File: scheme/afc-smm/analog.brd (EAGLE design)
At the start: 80 x 80 mm, 89 parts, among them IC1 OP1177R, IC10 LM2931-5.0, IC11 OP184, IC12 DAC8551, IC13 REF3033, IC14 317EMP, IC15 317EMP, IC2 TL082D, IC3 AD8515RJ, IC4 AD8615RJ, IC5 AD8221R, IC6 AD7476, IC7 REF3033, IC8 LM337LM, IC9 317EMP, J1 22-27-2031-03, J2 22-27-2021-02, Q1 IRLML2803, X1 BNC-206, X2 BNC-206

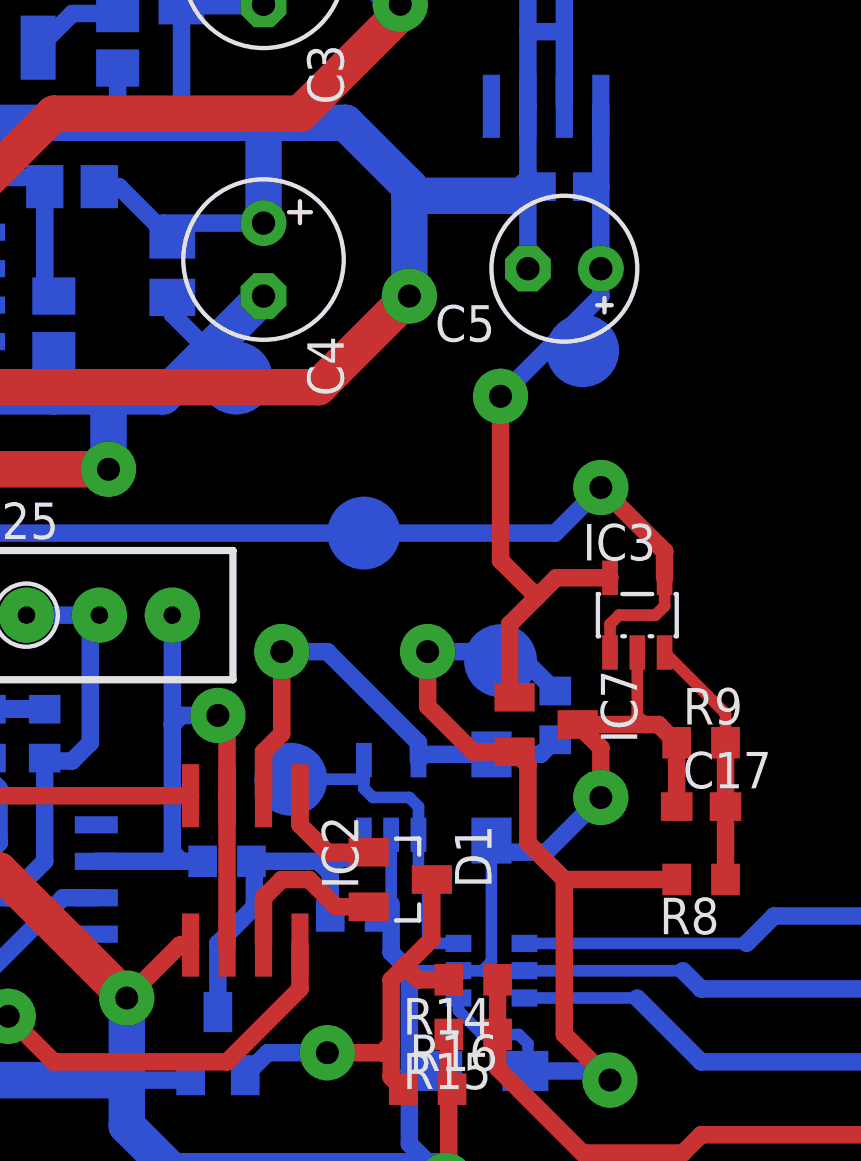
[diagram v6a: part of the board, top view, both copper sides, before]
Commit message: some bugfix after assembly, not all bugfix yet (capacitor for example and ground in dac)
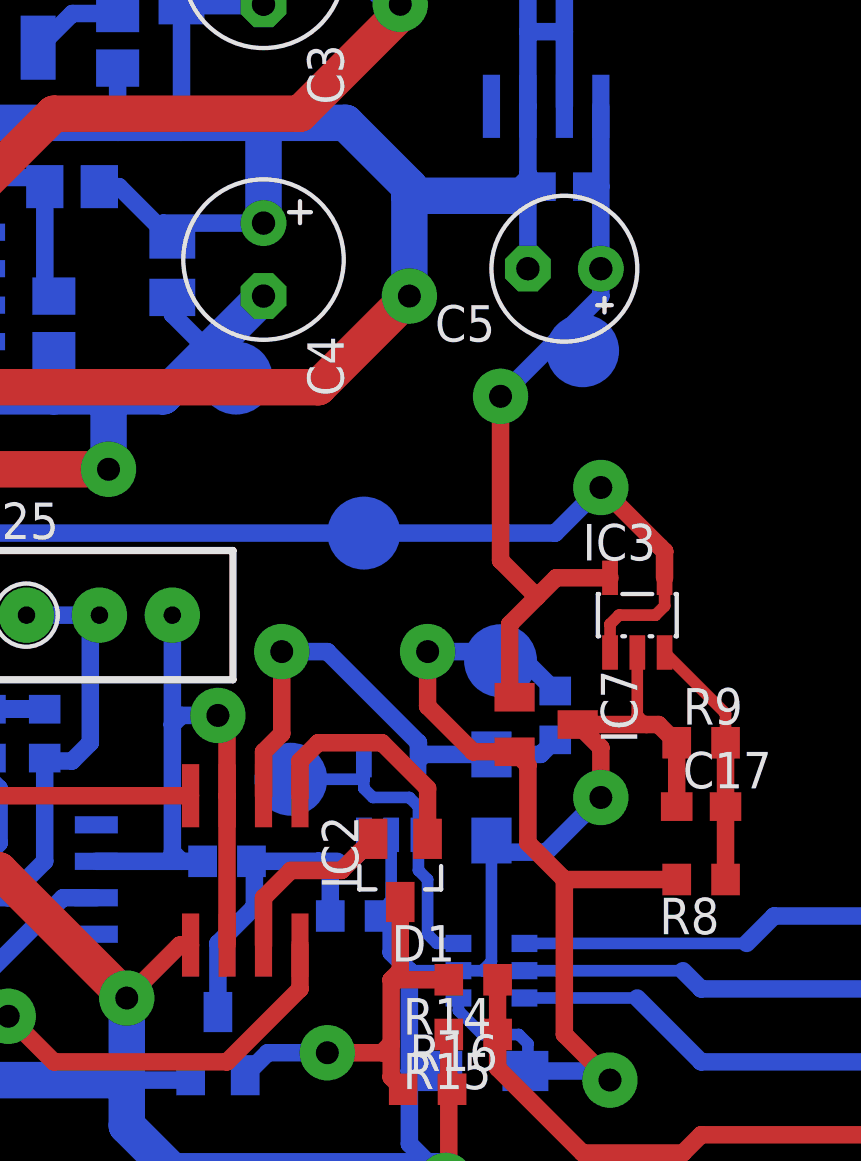
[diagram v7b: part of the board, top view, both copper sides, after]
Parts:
- moved D1 0.32 mm to (52.4, 42.5), turned to 180 degrees
- turned C8 to 0 degrees
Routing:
- net N$4: track 3.80 -> 8.33 mm
- net N$5: track 15.3 -> 14.4 mm
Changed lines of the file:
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@@
 <element name="IC1" library="linear" package="SOIC8" value="OP1177R" x="39.0525" y="42.2275" rot="MR90"/>
 <element name="IC2" library="linear" package="SO08" value="TL082D" x="46.99" y="42.545" rot="R180"/>
-<element name="D1" library="diode" package="SOT23" value="BAT54C" x="52.3875" y="42.2275" rot="R270"/>
+<element name="D1" library="diode" package="SOT23" value="BAT54C" x="52.3875" y="42.545" rot="R180"/>
 <element name="IC3" library="afc-smm" package="SOT23-5" value="AD8515RJ" x="60.6425" y="51.435">
 <attribute name="OC_NEWARK" value="88H0268" x="80.9625" y="-3.175" size="1.778" layer="27" display="off"/>
@@
 <element name="Q1" library="afc-smm" package="SOT23" value="IRLML2803" x="46.0375" y="36.5125" rot="MR0"/>
 <element name="C16" library="rcl" package="C0603" value="0.1" x="31.115" y="46.0375" rot="MR180"/>
-<element name="C8" library="rcl" package="C0603" value="0.1" x="58.1025" y="66.3575" rot="MR180"/>
+<element name="C8" library="rcl" package="C0603" value="0.1" x="58.1025" y="66.3575" rot="MR0"/>
 <element name="C12" library="rcl" package="C0603" value="0.1" x="62.5475" y="4.445" rot="MR270"/>
 <element name="C17" library="rcl" package="C0603" value="0.1" x="62.865" y="44.7675"/>
@@
 <wire x1="73.025" y1="63.3857" x2="72.6694" y2="63.7413" width="0.6096" layer="1"/>
 <contactref element="C8" pad="2"/>
-<wire x1="56.88375" y1="66.72625" x2="58.9525" y2="66.3575" width="0" layer="19" extent="16-16"/>
+<wire x1="57.2525" y1="66.3575" x2="56.8325" y2="66.3575" width="0.4064" layer="16"/>
 </signal>
 <signal name="N$1">
@@
 <contactref element="D1" pad="3"/>
 <contactref element="R14" pad="2"/>
-<wire x1="53.4875" y1="42.2275" x2="53.4875" y2="40.1525" width="0.6096" layer="1"/>
-<wire x1="53.4875" y1="40.1525" x2="52.54625" y2="39.21125" width="0.6096" layer="1"/>
-<wire x1="52.54625" y1="39.21125" x2="52.07" y2="38.735" width="0.6096" layer="1"/>
 <via x="49.8475" y="36.195" extent="1-16" drill="0.8" diameter="1.9304"/>
 <wire x1="52.07" y1="38.735" x2="52.07" y2="36.5125" width="0.6096" layer="1"/>
 <wire x1="52.07" y1="36.5125" x2="52.07" y2="35.345" width="0.6096" layer="1"/>
-<wire x1="54.0775" y1="38.735" x2="53.0225" y2="38.735" width="0.6096" layer="1"/>
-<wire x1="53.0225" y1="38.735" x2="52.54625" y2="39.21125" width="0.6096" layer="1"/>
+<wire x1="54.0775" y1="38.735" x2="52.07" y2="38.735" width="0.6096" layer="1"/>
 <wire x1="52.07" y1="35.345" x2="52.49" y2="34.925" width="0.6096" layer="1"/>
 <wire x1="49.8475" y1="36.195" x2="51.7525" y2="36.195" width="0.6096" layer="1"/>
@@
 <wire x1="49.8475" y1="36.195" x2="47.77" y2="36.195" width="0.6096" layer="16"/>
 <wire x1="47.77" y1="36.195" x2="46.9875" y2="35.4125" width="0.6096" layer="16"/>
+<wire x1="52.3875" y1="41.445" x2="52.3875" y2="39.0525" width="0.6096" layer="1"/>
+<wire x1="52.3875" y1="39.0525" x2="52.07" y2="38.735" width="0.6096" layer="1"/>
 </signal>
 <signal name="N$8">
@@
 <contactref element="D1" pad="1"/>
 <contactref element="IC2" pad="1"/>
-<wire x1="51.2875" y1="43.1775" x2="49.85" y2="43.1775" width="0.6096" layer="1"/>
-<wire x1="49.85" y1="43.1775" x2="48.895" y2="44.1325" width="0.6096" layer="1"/>
-<wire x1="48.895" y1="44.1325" x2="48.895" y2="45.145" width="0.6096" layer="1"/>
+<wire x1="48.895" y1="45.145" x2="48.895" y2="46.355" width="0.6096" layer="1"/>
+<wire x1="48.895" y1="46.355" x2="49.53" y2="46.99" width="0.6096" layer="1"/>
+<wire x1="49.53" y1="46.99" x2="51.7525" y2="46.99" width="0.6096" layer="1"/>
+<wire x1="51.7525" y1="46.99" x2="53.34" y2="45.4025" width="0.6096" layer="1"/>
+<wire x1="53.34" y1="45.4025" x2="53.34" y2="43.6475" width="0.6096" layer="1"/>
+<wire x1="53.34" y1="43.6475" x2="53.3375" y2="43.645" width="0.6096" layer="1"/>
 </signal>
 <signal name="N$6">
 <contactref element="D1" pad="2"/>
 <contactref element="IC2" pad="7"/>
-<wire x1="51.2875" y1="41.2775" x2="50.1625" y2="41.2775" width="0.6096" layer="1"/>
-<wire x1="50.1625" y1="41.2775" x2="49.2125" y2="42.2275" width="0.6096" layer="1"/>
-<wire x1="49.2125" y1="42.2275" x2="48.26" y2="42.2275" width="0.6096" layer="1"/>
-<wire x1="48.26" y1="42.2275" x2="47.625" y2="41.5925" width="0.6096" layer="1"/>
+<wire x1="48.5775" y1="42.545" x2="47.625" y2="41.5925" width="0.6096" layer="1"/>
 <wire x1="47.625" y1="41.5925" x2="47.625" y2="39.945" width="0.6096" layer="1"/>
+<wire x1="48.5775" y1="42.545" x2="50.3375" y2="42.545" width="0.6096" layer="1"/>
+<wire x1="50.3375" y1="42.545" x2="51.4375" y2="43.645" width="0.6096" layer="1"/>
 </signal>
 <signal name="-12V">
@@
 <wire x1="58.7375" y1="60.6425" x2="58.1025" y2="61.2775" width="0.6096" layer="16"/>
 <contactref element="C8" pad="1"/>
-<wire x1="59.3725" y1="66.3575" x2="57.2525" y2="66.3575" width="0" layer="19" extent="16-16"/>
+<wire x1="58.9525" y1="66.3575" x2="59.3725" y2="66.3575" width="0.4064" layer="16"/>
 </signal>
 <signal name="N$30">
